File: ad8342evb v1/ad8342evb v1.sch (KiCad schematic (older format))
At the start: 46 parts, among them J1 PWR_in_5V, J2 RF_in, J3 LO_in, J4 Gain_Jumper, J5 IF_out, U1 AD8342, U2 OPA2320

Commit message: changed LPF to Pi type
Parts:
- added C?: 10nF, symbol Device:C
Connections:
- wire segments 135 -> 138
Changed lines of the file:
@@
 $EndComp
-Wire Wire Line
-	8650 4250 8850 4250
 Wire Wire Line
 	9150 4250 9300 4250
@@
 Wire Wire Line
 	5450 1850 5450 1600
+$Comp
+L Device:C C?
+U 1 1 5F2E07FD
+P 8750 4550
+F 0 "C?" H 8865 4596 50  0000 L CNN
+F 1 "10nF" H 8865 4505 50  0000 L CNN
+F 2 "" H 8788 4400 50  0001 C CNN
+F 3 "~" H 8750 4550 50  0001 C CNN
+	1    8750 4550
+	1    0    0    -1
+$EndComp
+Wire Wire Line
+	8750 4250 8750 4400
+Wire Wire Line
+	8750 4700 8750 4800
+$Comp
+L power:GND #PWR?
+U 1 1 5F2E0805
+P 8750 4800
+F 0 "#PWR?" H 8750 4550 50  0001 C CNN
+F 1 "GND" H 8755 4627 50  0000 C CNN
+F 2 "" H 8750 4800 50  0001 C CNN
+F 3 "" H 8750 4800 50  0001 C CNN
+	1    8750 4800
+	1    0    0    -1
+$EndComp
+Wire Wire Line
+	8650 4250 8750 4250
+Connection ~ 8750 4250
+Wire Wire Line
+	8750 4250 8850 4250
 $EndSCHEMATC

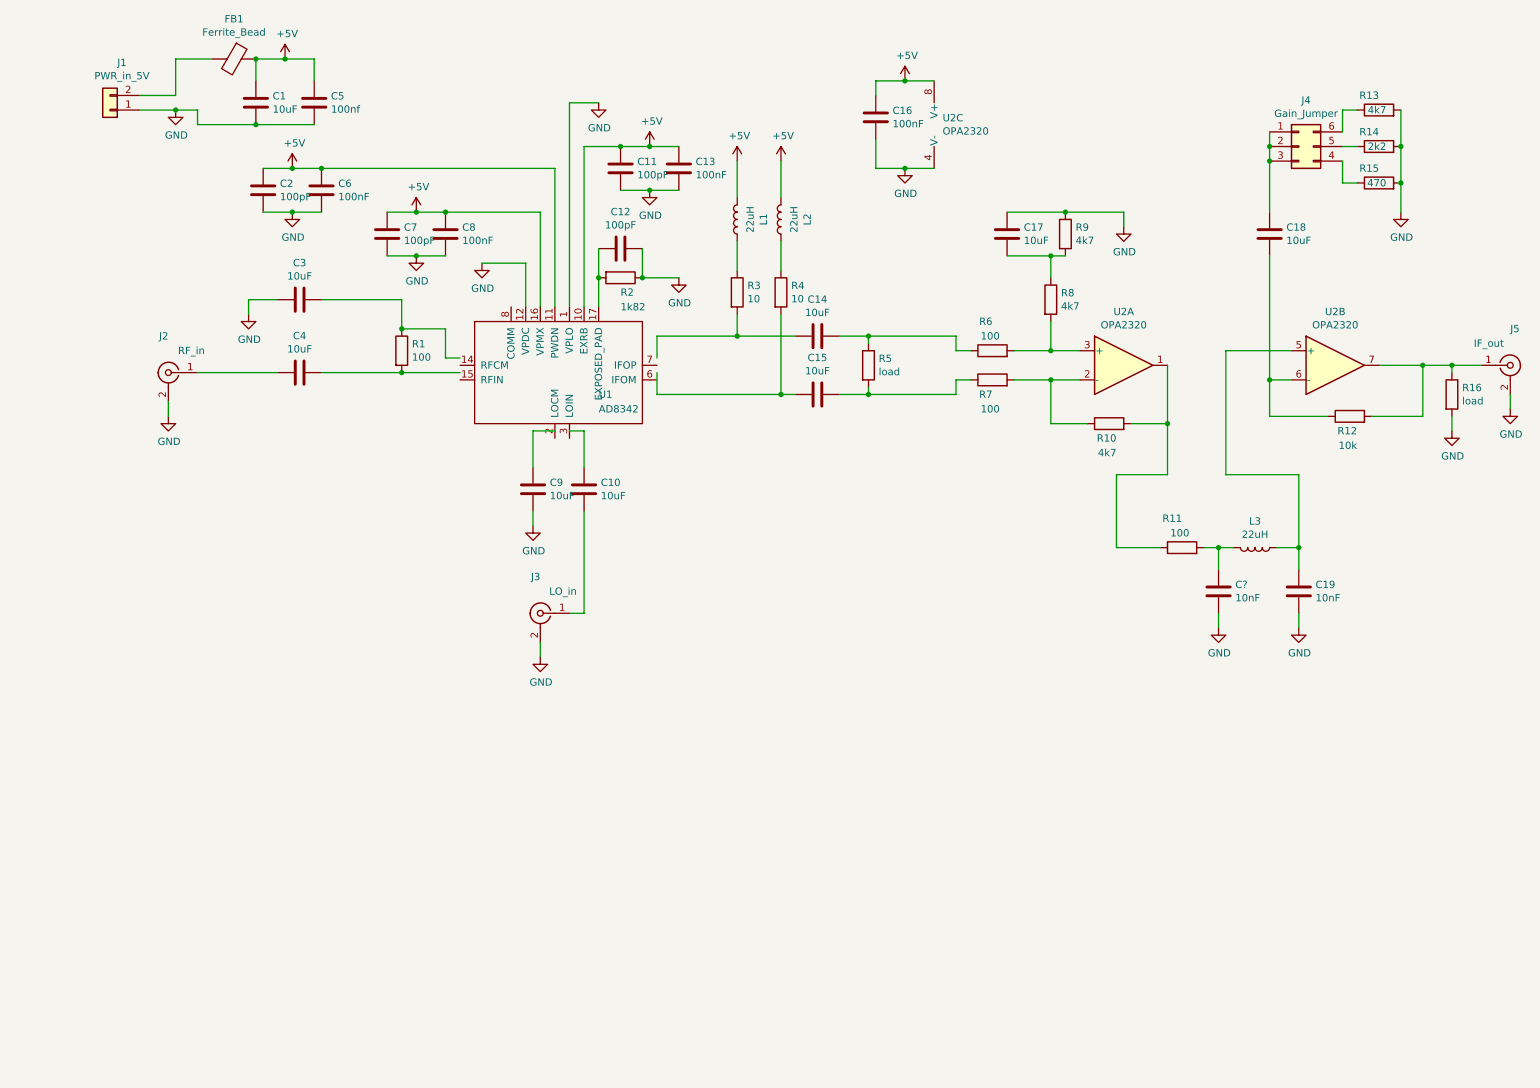
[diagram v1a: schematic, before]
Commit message: added different power options
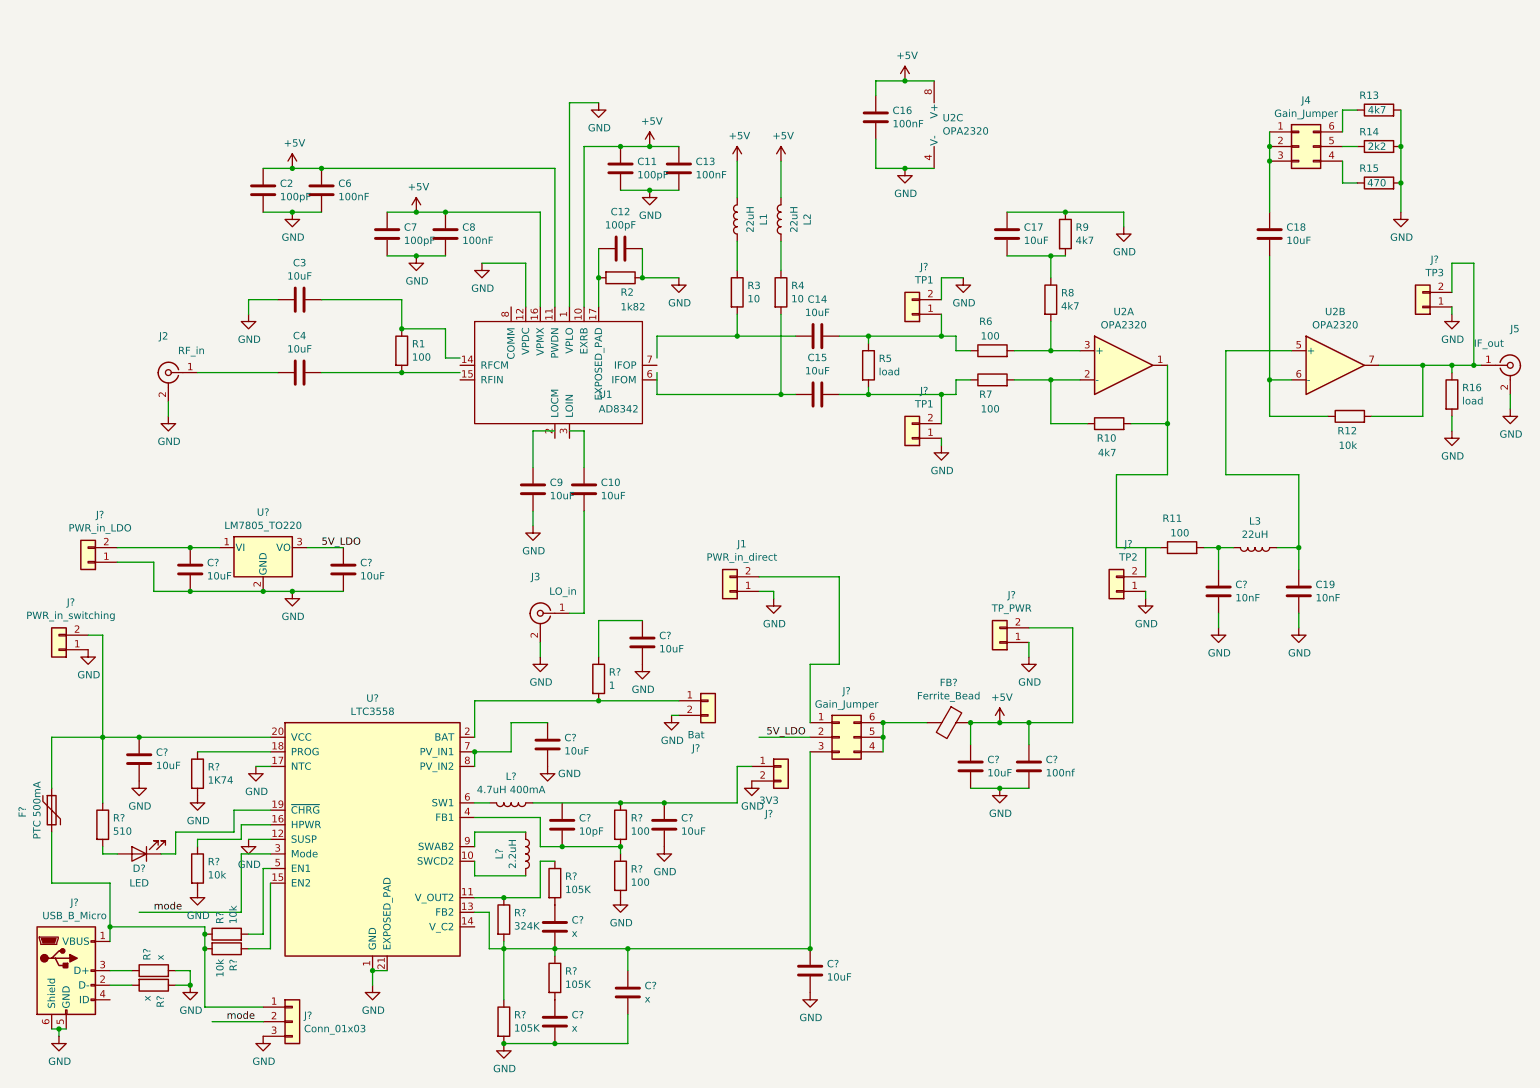
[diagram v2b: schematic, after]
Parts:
- removed C1: 10uF, symbol Device:C
- removed C5: 100nf, symbol Device:C
- removed FB1: Ferrite_Bead, symbol Device:Ferrite_Bead
- added C?: 100nf, symbol Device:C
- added C? (x8): 10uF, symbol Device:C
- added C? (x3): x, symbol Device:C
- added C?: 10pF, symbol Device:C
- added D?: LED, symbol Device:LED
- added F?: PTC 500mA, Fuse:Fuse_1812_4532Metric_Pad1.30x3.40mm_HandSolder, symbol Device:Polyfuse
- added FB?: Ferrite_Bead, symbol Device:Ferrite_Bead
- added J?: Gain_Jumper, symbol Connector_Generic:Conn_02x03_Counter_Clockwise
- added J?: PWR_in_LDO, symbol Connector_Generic:Conn_01x02
- added J?: PWR_in_switching, symbol Connector_Generic:Conn_01x02
- added J? (x2): TP1, symbol Connector_Generic:Conn_01x02
- added J?: TP2, symbol Connector_Generic:Conn_01x02
- added J?: TP3, symbol Connector_Generic:Conn_01x02
- added J?: TP_PWR, symbol Connector_Generic:Conn_01x02
- added J?: Bat, symbol Connector_Generic:Conn_01x02
- added J?: USB_B_Micro, Connector_USB:USB_Micro-B_Molex-105017-0001, symbol Connector:USB_B_Micro
- added J?: 3V3, symbol Connector_Generic:Conn_01x02
- added J?: Conn_01x03, symbol Connector_Generic:Conn_01x03
- added L?: 2.2uH, symbol Device:L
- added L?: 4.7uH 400mA, symbol Device:L
- added R?: 1K74, symbol Device:R
- added R? (x2): 100, symbol Device:R
- added R?: 1, symbol Device:R
- added R?: 324K, symbol Device:R
- added R? (x3): 105K, symbol Device:R
- added R?: 510, symbol Device:R
- added R? (x3): 10k, symbol Device:R
- added R? (x2): x, symbol Device:R
- added U?: LM7805_TO220, Package_TO_SOT_THT:TO-220-3_Vertical, symbol Regulator_Linear:LM7805_TO220
- added U?: LTC3558, Package_DFN_QFN:QFN-20-1EP_3x3mm_P0.4mm_EP1.65x1.65mm, symbol user_Battery_Management:LTC3558
- J1: value PWR_in_5V -> PWR_in_direct
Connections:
- net labels added: 5V_LDO, mode
- wire segments 138 -> 261
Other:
- moved on the sheet: J1

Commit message: finished layout
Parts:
- removed J4, J?: Gain_Jumper, symbol Connector_Generic:Conn_02x03_Counter_Clockwise
- added D2: PWR_LED, LED_SMD:LED_0805_2012Metric_Pad1.15x1.40mm_HandSolder, symbol Device:LED
- added D3: PWR_LED_3V3, LED_SMD:LED_0805_2012Metric_Pad1.15x1.40mm_HandSolder, symbol Device:LED
- added J12: PWR_Jumper, Connector_PinHeader_2.54mm:PinHeader_2x03_P2.54mm_Vertical, symbol Connector_Generic:Conn_02x03_Odd_Even
- added J4: Gain_Jumper, Connector_PinHeader_2.54mm:PinHeader_2x03_P2.54mm_Vertical, symbol Connector_Generic:Conn_02x03_Odd_Even
- added R31, R32: 510, Resistor_SMD:R_0805_2012Metric_Pad1.15x1.40mm_HandSolder, symbol Device:R
- C1, C20, C21, C24, C26, C27, C28, C29, C5: renamed from C?; footprint (none) -> Capacitor_SMD:C_0805_2012Metric_Pad1.15x1.40mm_HandSolder
- C10, C11, C12, C13, C14, C15, C16, C17, C18, C19, C2, C3, C4, C6, C7, C8, C9: footprint (none) -> Capacitor_SMD:C_0805_2012Metric_Pad1.15x1.40mm_HandSolder
- C22: renamed from C?; value x -> 33pF; footprint (none) -> Capacitor_SMD:C_0805_2012Metric_Pad1.15x1.40mm_HandSolder
- C23: renamed from C?; value x -> 330pF; footprint (none) -> Capacitor_SMD:C_0805_2012Metric_Pad1.15x1.40mm_HandSolder
- C25: renamed from C?; value x -> 10pF; footprint (none) -> Capacitor_SMD:C_0805_2012Metric_Pad1.15x1.40mm_HandSolder
- C30: renamed from C?; value 100nf -> 100nF; footprint (none) -> Capacitor_SMD:C_0805_2012Metric_Pad1.15x1.40mm_HandSolder
- C31: renamed from C?; value 10nF -> empty; footprint (none) -> Capacitor_SMD:C_0805_2012Metric_Pad1.15x1.40mm_HandSolder
- D1: renamed from D?; value LED -> CHARGE_LED; footprint (none) -> LED_SMD:LED_0805_2012Metric_Pad1.15x1.40mm_HandSolder
- FB1: renamed from FB?; footprint (none) -> Inductor_SMD:L_0805_2012Metric_Pad1.15x1.40mm_HandSolder
- J1: footprint (none) -> Connector_PinHeader_2.54mm:PinHeader_1x02_P2.54mm_Vertical
- J10, J11, J6, J8: renamed from J?; footprint (none) -> Connector_PinHeader_2.54mm:PinHeader_1x02_P2.54mm_Vertical
- J13, J14, J15, J16, J17: renamed from J?; footprint (none) -> TestPoint:TestPoint_2Pads_Pitch2.54mm_Drill0.8mm
- J2, J3, J5: footprint (none) -> Connector_Coaxial:SMA_Amphenol_132134_Vertical
- J7: renamed from J?; value USB_B_Micro -> PWR_in_USB
- J9: renamed from J?; value Conn_01x03 -> Mode_Jumper; footprint (none) -> Connector_PinHeader_2.54mm:PinHeader_1x03_P2.54mm_Vertical
- L1, L2, L3: footprint (none) -> Inductor_SMD:L_1008_2520Metric
- L4, L5: renamed from L?; footprint (none) -> Inductor_SMD:L_1008_2520Metric
- R1, R10, R11, R12, R15, R16, R2, R3, R4, R5, R6, R7, R8, R9: footprint (none) -> Resistor_SMD:R_0805_2012Metric_Pad1.15x1.40mm_HandSolder
- R13: value 4k7 -> 4K7; footprint (none) -> Resistor_SMD:R_0805_2012Metric_Pad1.15x1.40mm_HandSolder
- R14: value 2k2 -> 2K2; footprint (none) -> Resistor_SMD:R_0805_2012Metric_Pad1.15x1.40mm_HandSolder
- R17, R20, R21, R22, R23, R28: renamed from R?; footprint (none) -> Resistor_SMD:R_0805_2012Metric_Pad1.15x1.40mm_HandSolder
- R18, R19: renamed from R?; value x -> 10K; footprint (none) -> Resistor_SMD:R_0805_2012Metric_Pad1.15x1.40mm_HandSolder
- R24: renamed from R?; value 324K -> 1M05; footprint (none) -> Resistor_SMD:R_0805_2012Metric_Pad1.15x1.40mm_HandSolder
- R25: renamed from R?; value 105K -> 200K; footprint (none) -> Resistor_SMD:R_0805_2012Metric_Pad1.15x1.40mm_HandSolder
- R26: renamed from R?; value 105K -> 300K; footprint (none) -> Resistor_SMD:R_0805_2012Metric_Pad1.15x1.40mm_HandSolder
- R27: renamed from R?; value 105K -> 77K; footprint (none) -> Resistor_SMD:R_0805_2012Metric_Pad1.15x1.40mm_HandSolder
- R29: renamed from R?; value 100 -> 619k; footprint (none) -> Resistor_SMD:R_0805_2012Metric_Pad1.15x1.40mm_HandSolder
- R30: renamed from R?; value 100 -> 200K; footprint (none) -> Resistor_SMD:R_0805_2012Metric_Pad1.15x1.40mm_HandSolder
- U4: renamed from U1; footprint (none) -> user_Package_CSP:LFCSP-16-1EP_3x3mm_P0.5mm_EP1.6x1.6mm
- gave numbers to parts that had none: 3
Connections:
- net labels added: 3V3, 5V_Switching
- wire segments 261 -> 277
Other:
- note added: "Filter values are estimates"
- moved on the sheet: C12, C27, C3, C4, D1, J2, R1, R17, R2, R20, R25, U4

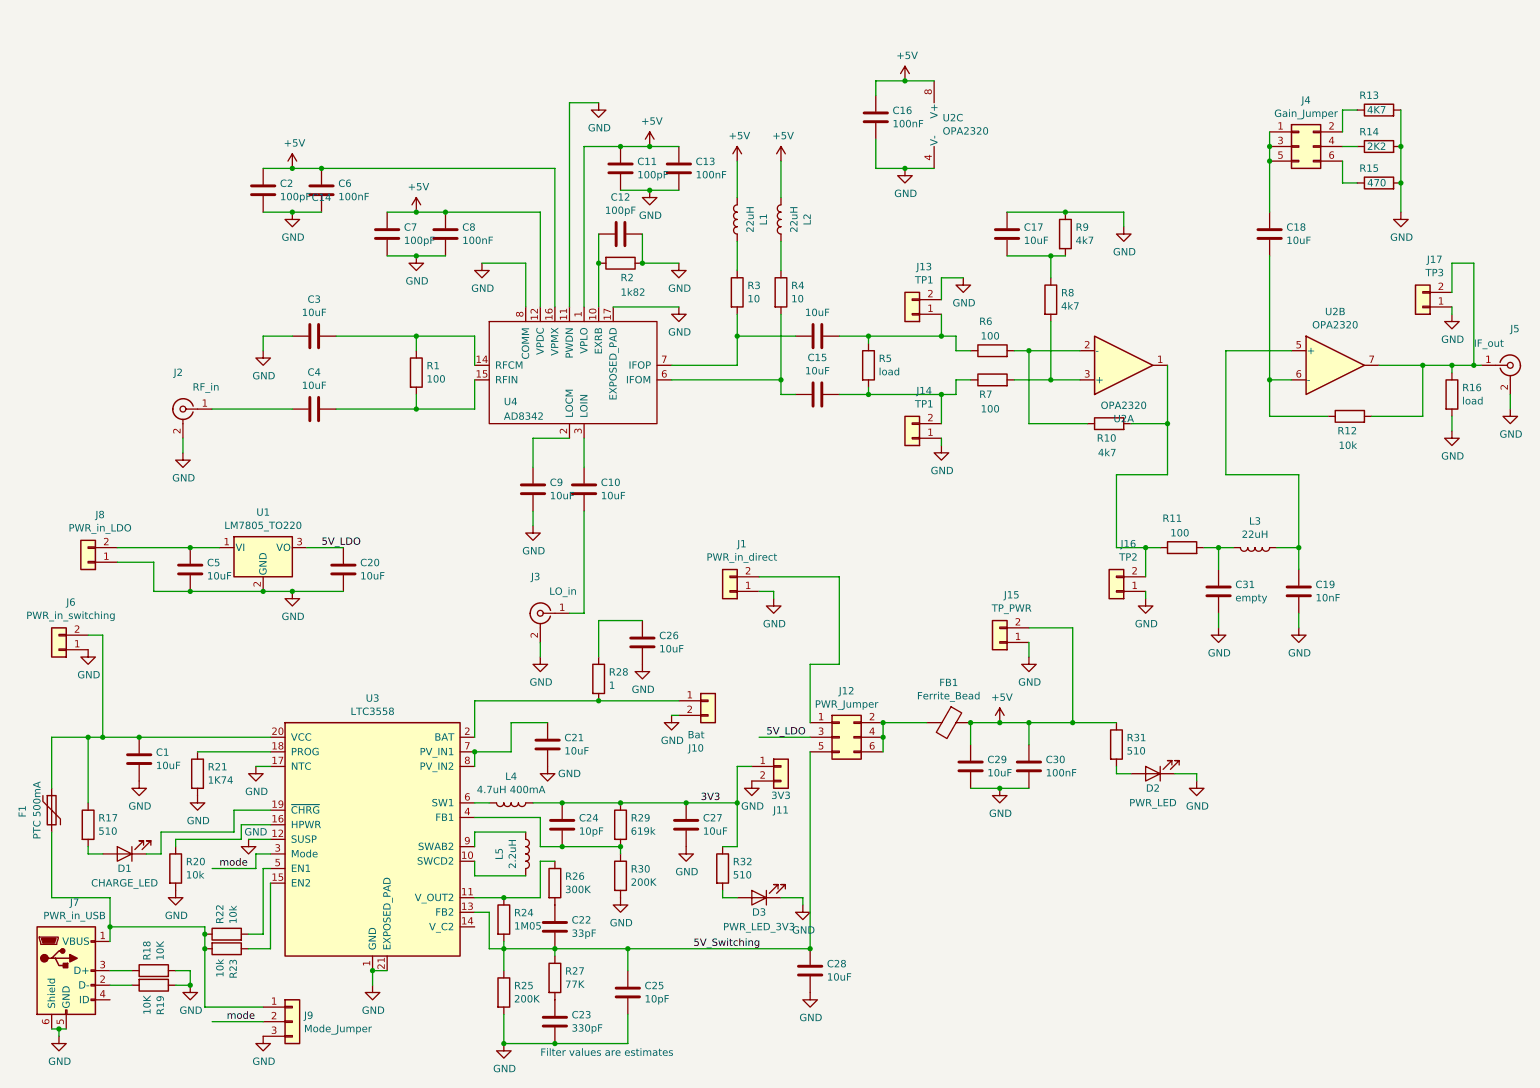
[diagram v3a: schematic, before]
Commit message: added separate GNDA plane
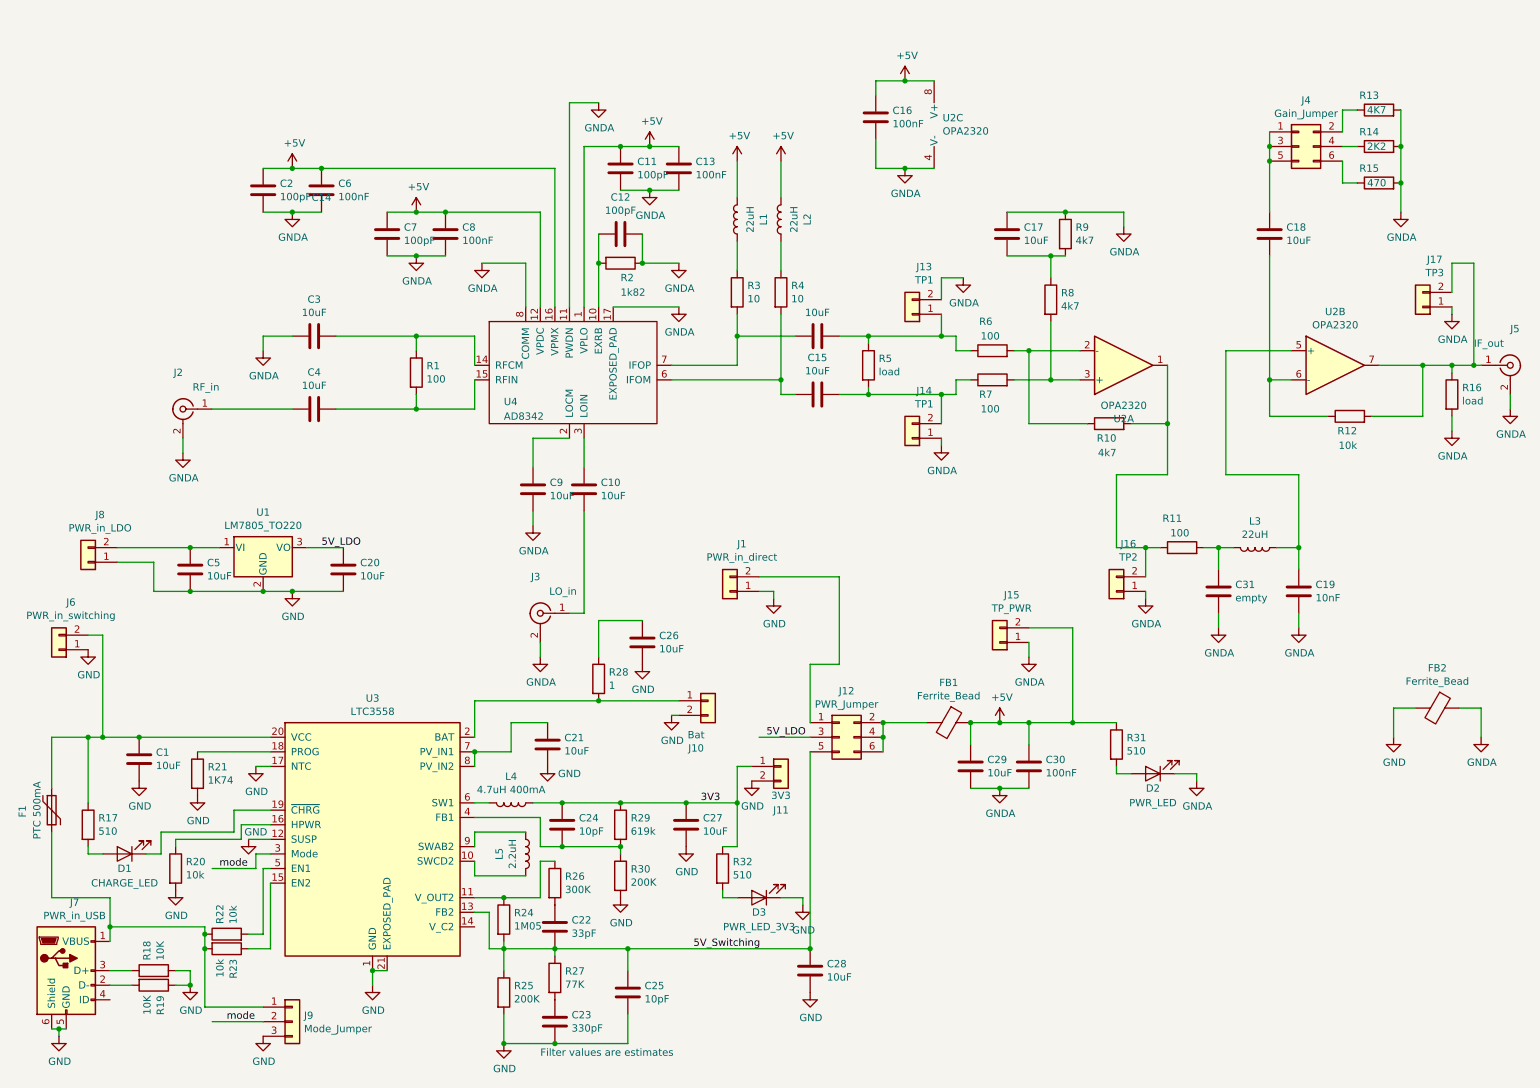
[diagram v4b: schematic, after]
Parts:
- added FB2: Ferrite_Bead, Inductor_SMD:L_0805_2012Metric_Pad1.15x1.40mm_HandSolder, symbol Device:Ferrite_Bead
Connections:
- net GND: now also FB2.2; no longer C11.2, C12.1, C13.2, C16.2, C17.1, C19.2, C2.2, C29.2, C3.2, C30.2, C31.2, C6.2, C7.2, C8.2, C9.2, D2.1 (K), J13.2 (Pin_2), J14.1 (Pin_1), J15.1 (Pin_1), J16.1 (Pin_1), J17.1 (Pin_1), J2.2 (Ext), J3.2 (Ext), J5.2 (Ext), R13.2, R14.2, R15.2, R16.2, R2.1, R9.1, U2.4 (V-), U4.11 (PWDN), U4.13 (COMM), U4.17 (EXPOSED_PAD), U4.4 (COMM), U4.5 (COMM), U4.8 (COMM), U4.9 (COMM)
- new net GNDA: C11.2, C12.1, C13.2, C16.2, C17.1, C19.2, C2.2, C29.2, C3.2, C30.2, C31.2, C6.2, C7.2, C8.2, C9.2, D2.1 (K), FB2.1, J13.2 (Pin_2), J14.1 (Pin_1), J15.1 (Pin_1), J16.1 (Pin_1), J17.1 (Pin_1), J2.2 (Ext), J3.2 (Ext), J5.2 (Ext), R13.2, R14.2, R15.2, R16.2, R2.1, R9.1, U2.4 (V-), U4.11 (PWDN), U4.13 (COMM), U4.17 (EXPOSED_PAD), U4.4 (COMM), U4.5 (COMM), U4.8 (COMM), U4.9 (COMM)
